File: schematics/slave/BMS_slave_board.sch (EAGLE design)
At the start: 53 parts, among them IC2 LT1021S, J1 AVR_SPI_PRG_6NS, Q1 BUZ10, Q2 BUZ10, Q3 BUZ10, Q4 BUZ10, U1 LMV324, U2 LMV324

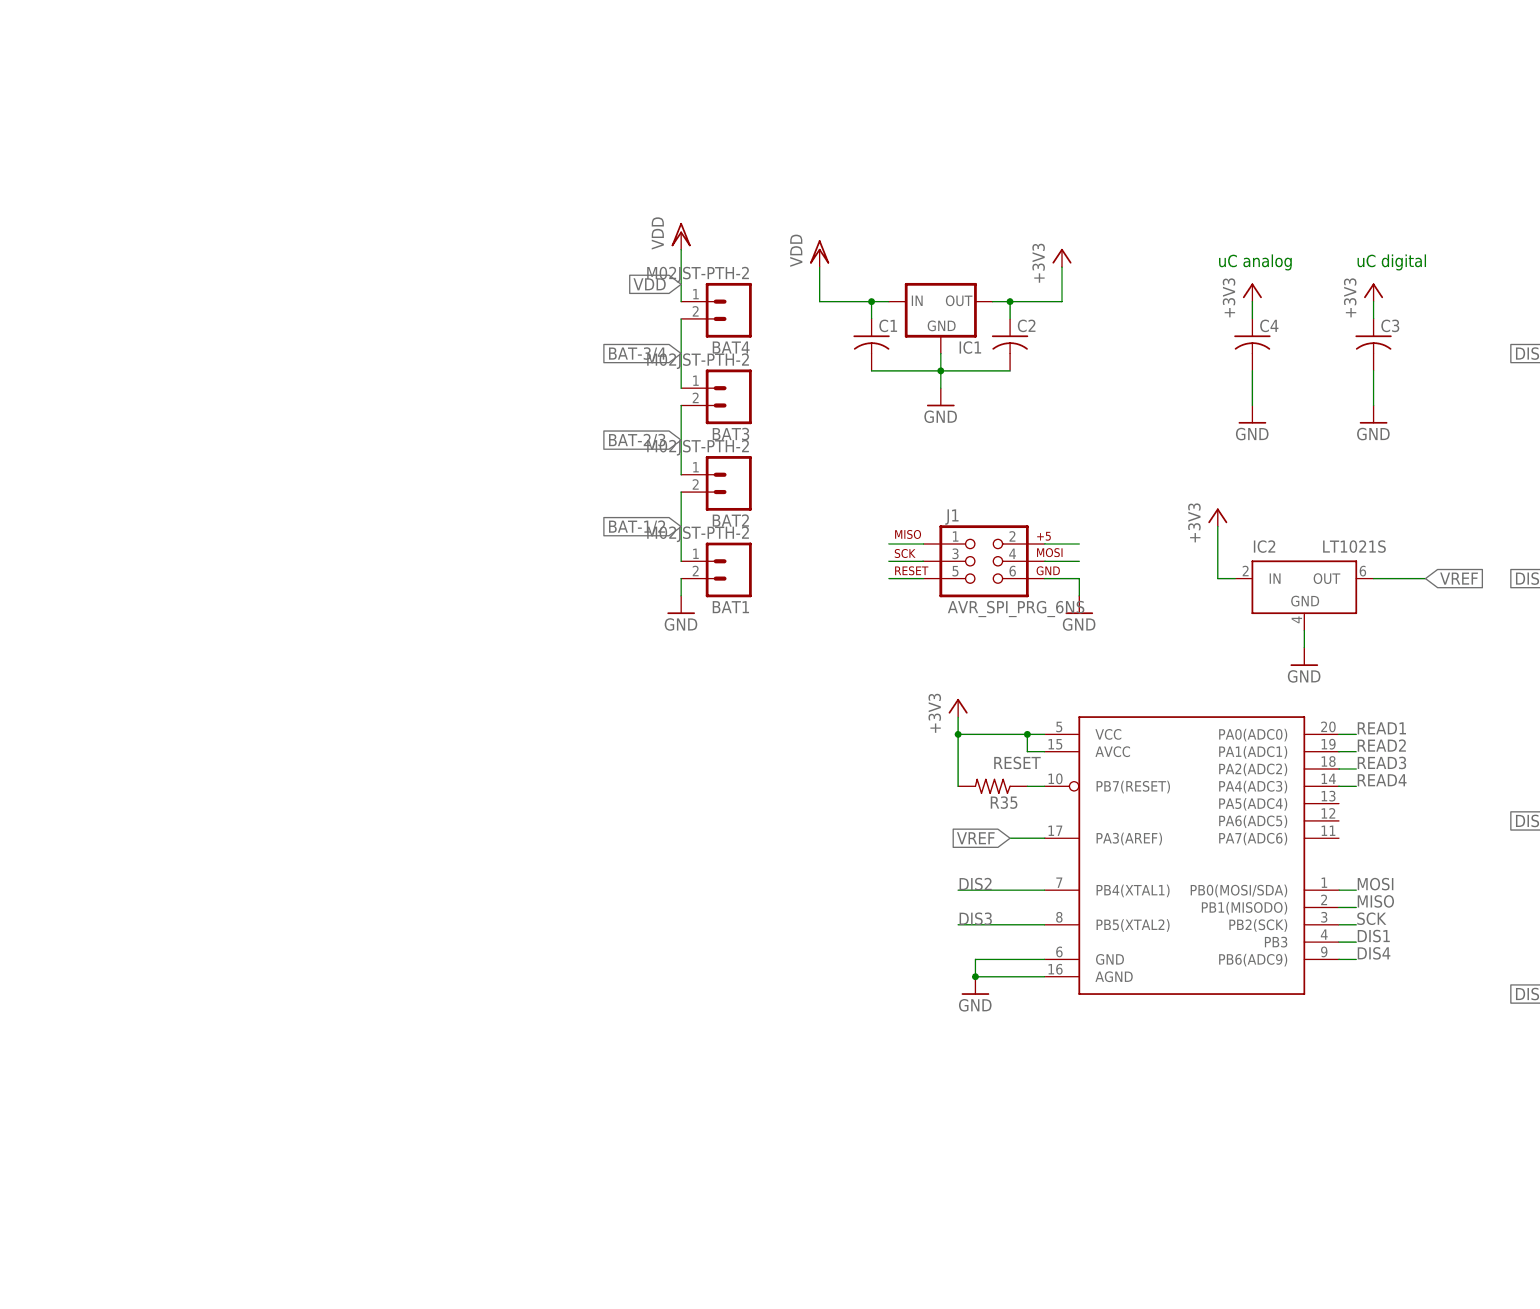
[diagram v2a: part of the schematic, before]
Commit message: added optoisolators and Master supply for optos
optos belong on slave to prevent a wide variety of voltages on master
but may be moved for space considerations. If we move 'em we have to
feed ground and power from each slave to the master.
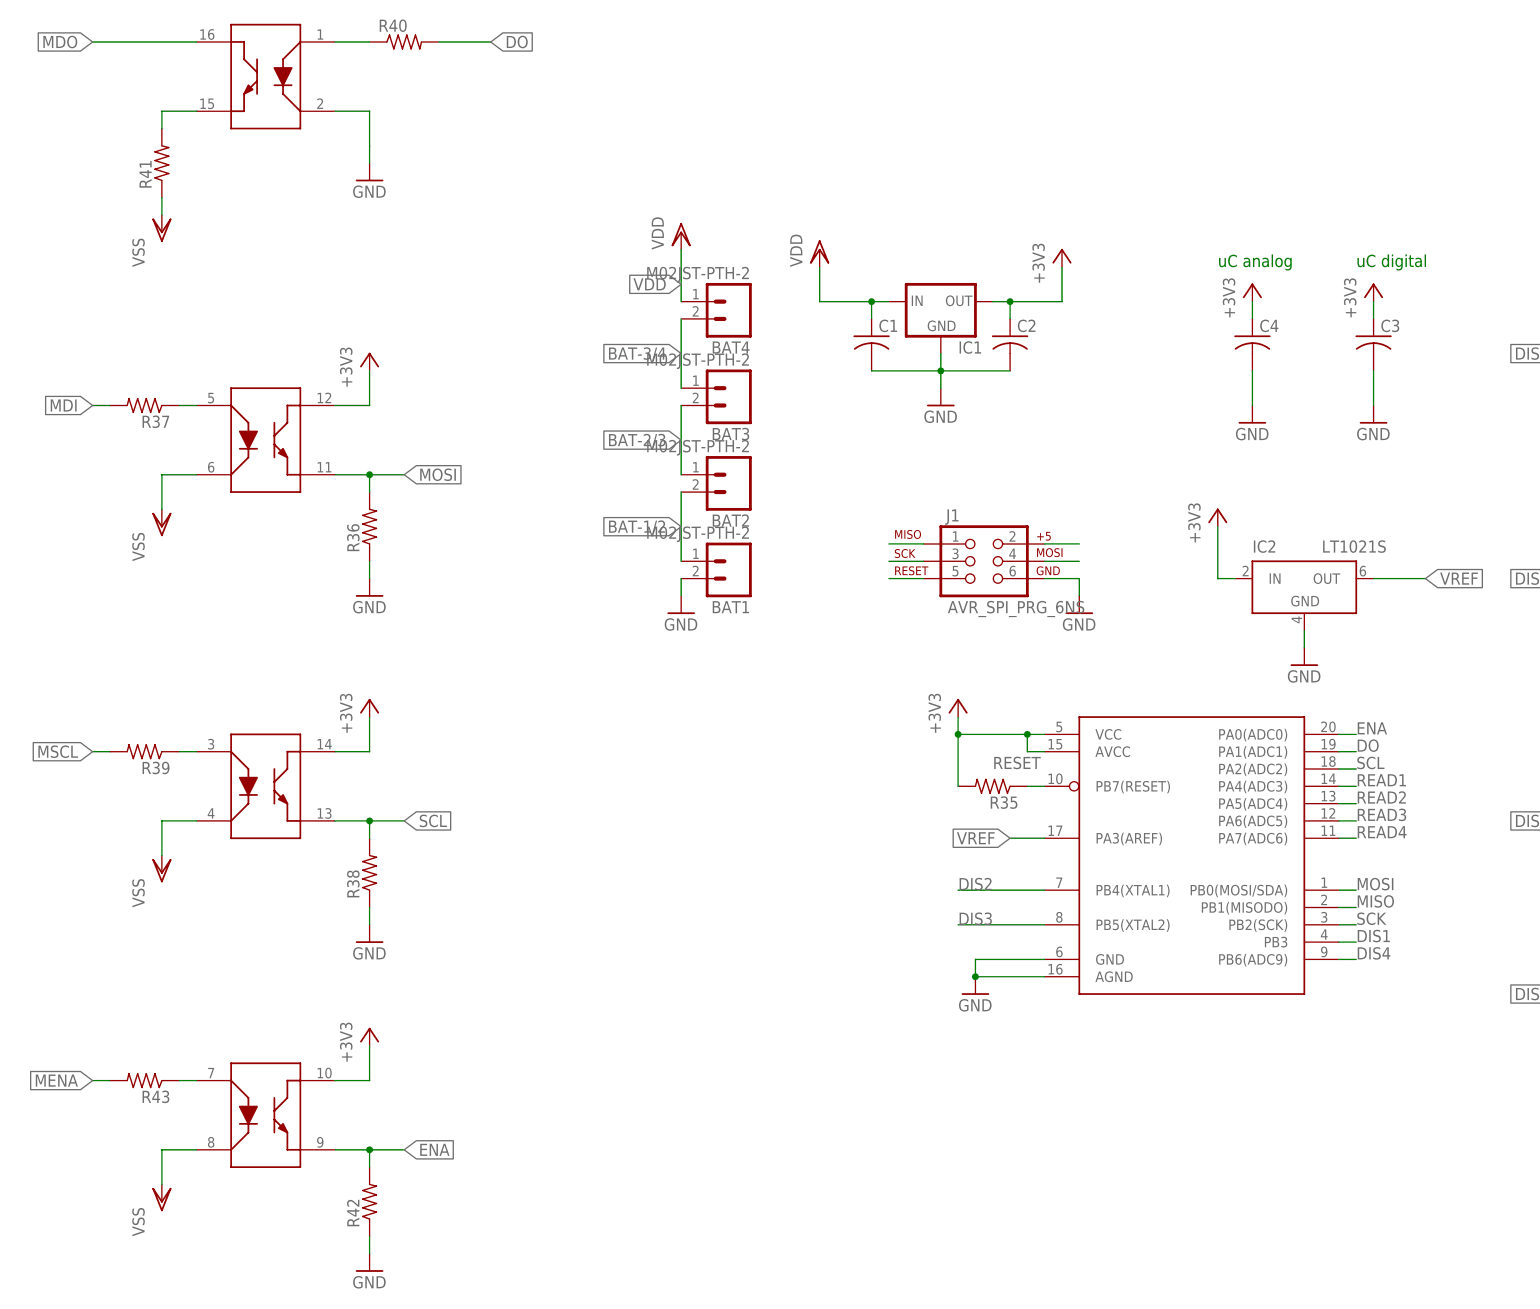
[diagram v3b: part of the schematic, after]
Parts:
- added R36, R37, R38, R39, R40, R41, R42, R43: (no value), rcl:R-US_0204/7
- added U$2: LTV-847, EVT-Eagle-Library:LTV-847
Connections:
- new net DO: R40.2, U$1.PA1(ADC1)
- new net ENA: R42.2, U$1.PA0(ADC0), U$2G$4.E
- new net MDI: R37.2
- new net MDO: U$2G$1.CO
- new net MENA: R43.2
- new net MSCL: R39.2
- new net N$23: R37.1, U$2G$3.A
- new net N$25: R39.1, U$2G$2.A
- new net N$28: R40.1, U$2G$1.A
- new net N$29: R41.2, U$2G$1.E
- new net N$31: R43.1, U$2G$4.A
- new net SCL: R38.2, U$1.PA2(ADC2), U$2G$2.E
- new net VSS: R41.1, U$2G$2.CA, U$2G$3.CA, U$2G$4.CA
- net +3V3: now also U$2G$2.CO, U$2G$3.CO, U$2G$4.CO
- net GND: now also R36.1, R38.1, R42.1, U$2G$1.CA
- net MOSI: now also R36.2, U$2G$3.E
- net READ1: now also U$1.PA4(ADC3); no longer U$1.PA0(ADC0)
- net READ2: now also U$1.PA5(ADC4); no longer U$1.PA1(ADC1)
- net READ3: now also U$1.PA6(ADC5); no longer U$1.PA2(ADC2)
- net READ4: now also U$1.PA7(ADC6); no longer U$1.PA4(ADC3)

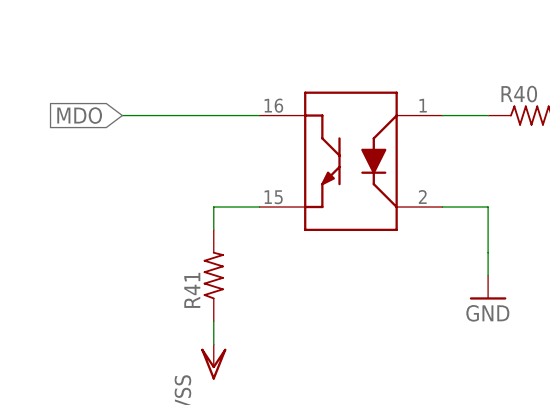
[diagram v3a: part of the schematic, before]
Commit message: added maste supply
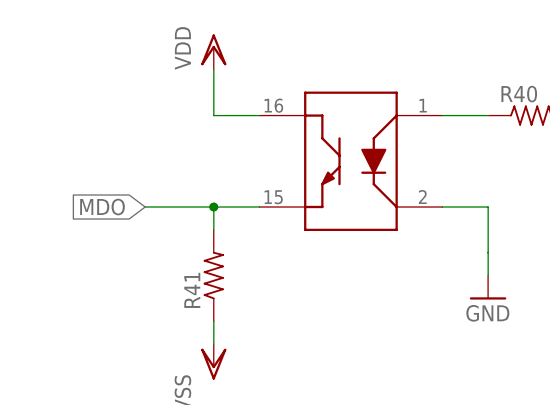
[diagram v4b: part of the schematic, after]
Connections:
- removed net N$29: R41.2, U$2G$1.E
- net MDO: now also R41.2, U$2G$1.E; no longer U$2G$1.CO
- net VDD: now also U$2G$1.CO
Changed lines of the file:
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@@
 <part name="VSS4" library="supply1" deviceset="VSS" device=""/>
 <part name="GND23" library="supply1" deviceset="GND" device=""/>
+<part name="VDD3" library="supply1" deviceset="VDD" device=""/>
 </parts>
 <sheets>
@@
 <instance part="U$2" gate="G$4" x="-170.18" y="-5.08" rot="R270"/>
 <instance part="GND23" gate="1" x="-154.94" y="132.08"/>
+<instance part="VDD3" gate="G$1" x="-185.42" y="160.02"/>
 </instances>
 <busses>
@@
 <pinref part="VDD2" gate="G$1" pin="VDD"/>
 </segment>
+<segment>
+<pinref part="U$2" gate="G$1" pin="CO"/>
+<wire x1="-180.34" y1="152.4" x2="-185.42" y2="152.4" width="0.1524" layer="91"/>
+<wire x1="-185.42" y1="152.4" x2="-185.42" y2="157.48" width="0.1524" layer="91"/>
+<pinref part="VDD3" gate="G$1" pin="VDD"/>
+</segment>
 </net>
 <net name="MOSI" class="0">
@@
 </segment>
 </net>
-<net name="N$29" class="0">
-<segment>
-<pinref part="U$2" gate="G$1" pin="E"/>
-<pinref part="R41" gate="G$1" pin="2"/>
-<wire x1="-180.34" y1="142.24" x2="-185.42" y2="142.24" width="0.1524" layer="91"/>
-<wire x1="-185.42" y1="142.24" x2="-185.42" y2="139.7" width="0.1524" layer="91"/>
-</segment>
-</net>
 <net name="VSS" class="0">
 <segment>
@@
 <net name="MDO" class="0">
 <segment>
-<pinref part="U$2" gate="G$1" pin="CO"/>
-<wire x1="-180.34" y1="152.4" x2="-195.58" y2="152.4" width="0.1524" layer="91"/>
-<label x="-195.58" y="152.4" size="1.778" layer="95" rot="R180" xref="yes"/>
-</segment>
-</net>
+<label x="-193.04" y="142.24" size="1.778" layer="95" rot="R180" xref="yes"/>
+<pinref part="U$2" gate="G$1" pin="E"/>
+<pinref part="R41" gate="G$1" pin="2"/>
+<wire x1="-185.42" y1="142.24" x2="-193.04" y2="142.24" width="0.1524" layer="91"/>
+<wire x1="-180.34" y1="142.24" x2="-185.42" y2="142.24" width="0.1524" layer="91"/>
+<wire x1="-185.42" y1="142.24" x2="-185.42" y2="139.7" width="0.1524" layer="91"/>
+<junction x="-185.42" y="142.24"/>
+</segment>
+</net>
